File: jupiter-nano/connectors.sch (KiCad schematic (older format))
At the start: 21 parts, among them J1 USB_B_Micro, J10 Conn_02x05_Odd_Even, J2 USB_B_Micro, J4 USB_B_Micro, J5 Micro_SD_Card_Det_Hirose_DM3AT, J6 Conn_01x02

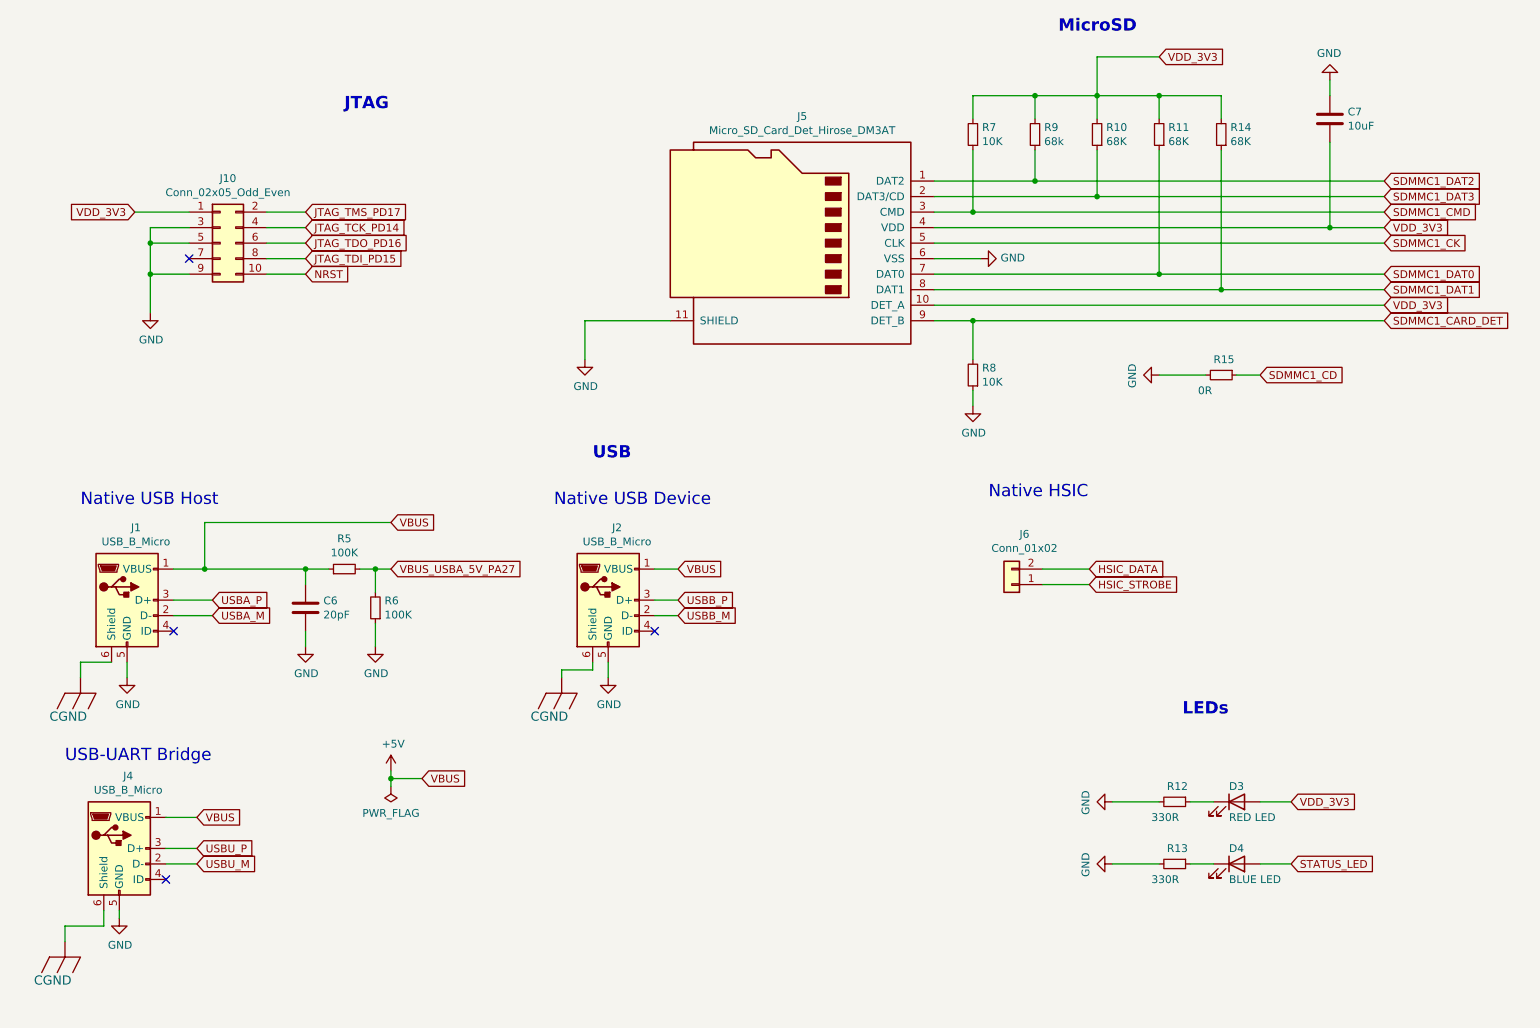
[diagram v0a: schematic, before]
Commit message: reorganized connector sheet
- and library location change
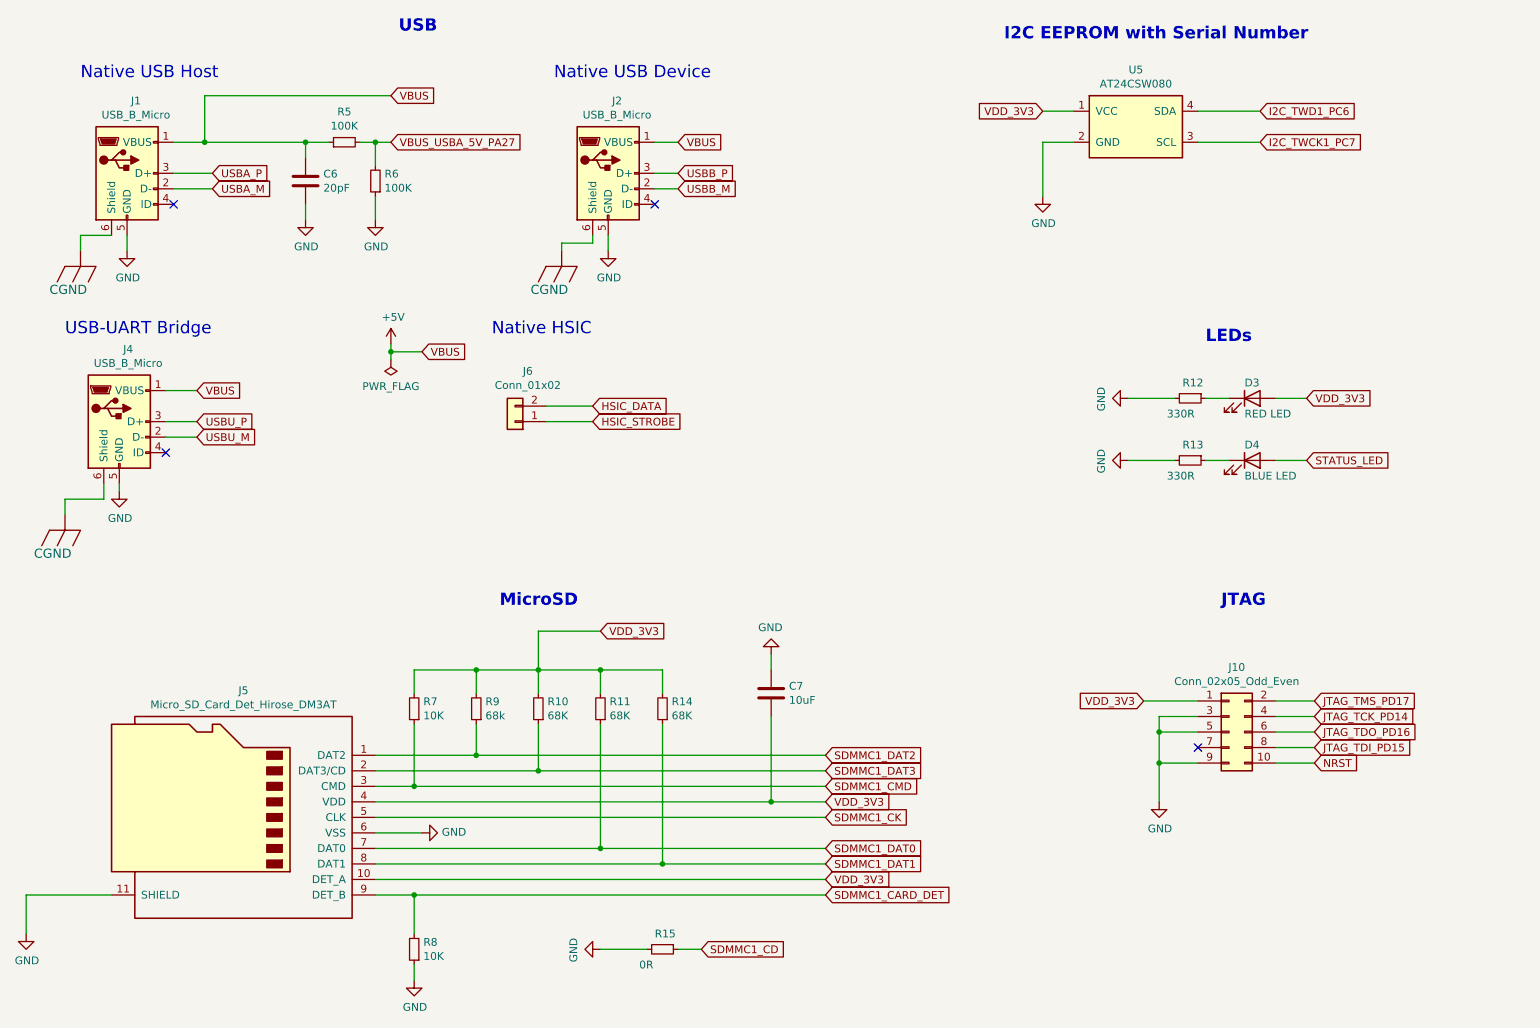
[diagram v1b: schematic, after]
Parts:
- added U5: AT24CSW080, symbol at24csw080:AT24CSW080
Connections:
- net GND: now also U5.2 (GND)
- net VDD_3V3: now also U5.1 (VCC)
- new net I2C_TWCK1_PC7: U5.3 (SCL)
- new net I2C_TWD1_PC6: U5.4 (SDA)
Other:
- note added: "I2C EEPROM with Serial Number"
- moved on the sheet: C6, C7, D3, D4, J1, J10, J2, J4, J5, J6, R10, R11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
